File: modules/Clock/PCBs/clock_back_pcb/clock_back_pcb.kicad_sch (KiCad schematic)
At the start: 6 parts, among them J10 Conn_01x11_Pin, J11 Eurorack_2x8_Power, J9 Conn_01x08_Socket

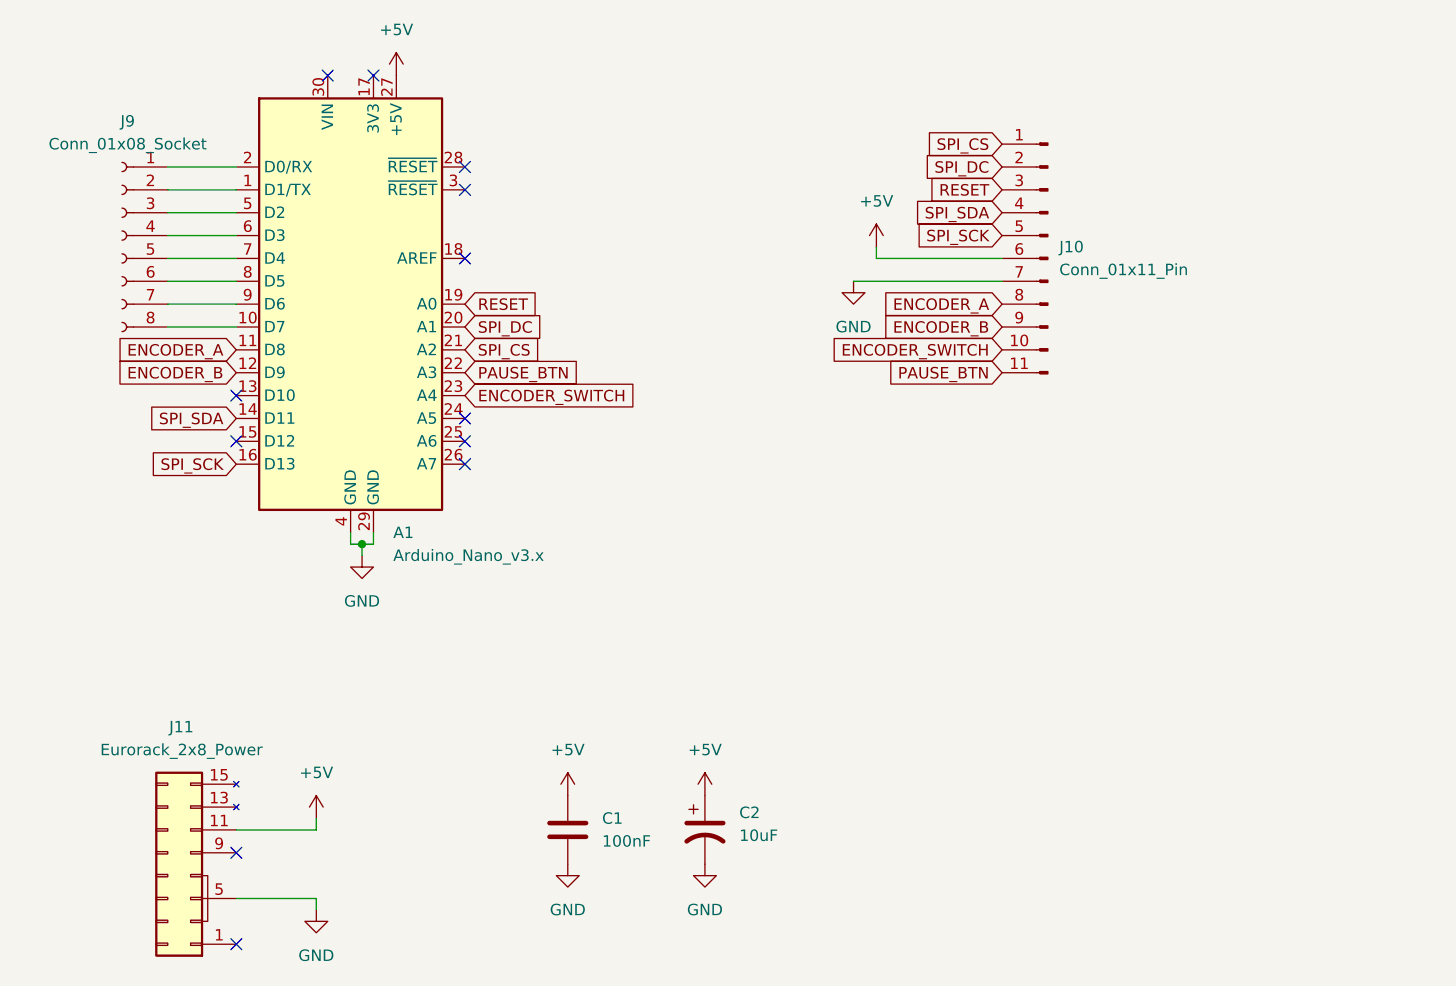
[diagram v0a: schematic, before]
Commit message: tweak clock faceplate
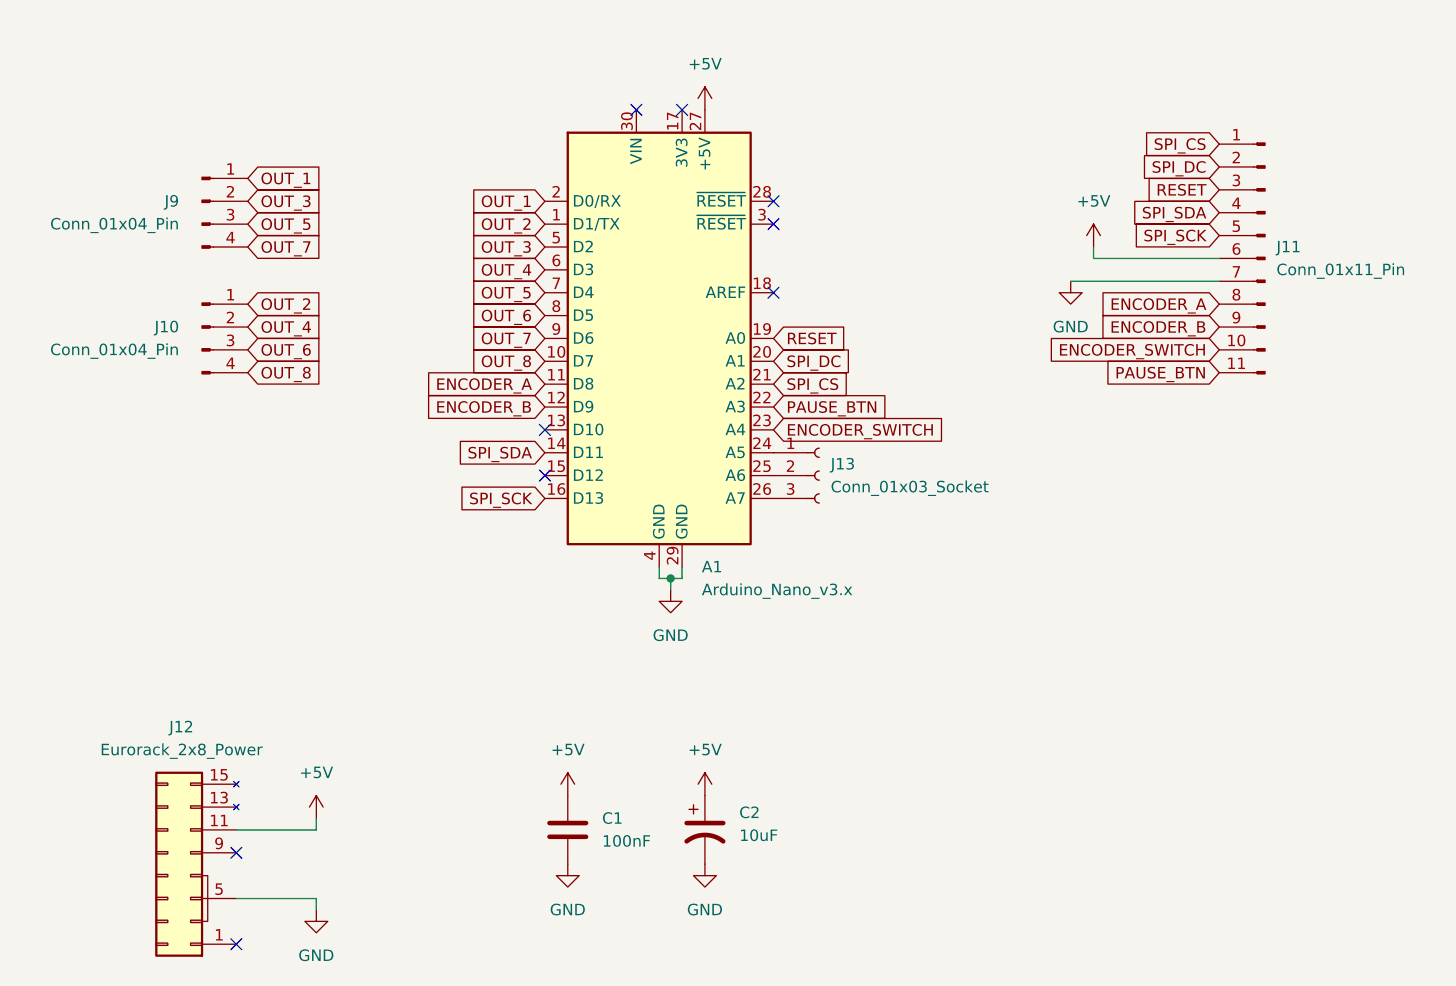
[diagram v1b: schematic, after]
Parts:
- removed J9: Conn_01x08_Socket, Connector_PinHeader_2.54mm:PinHeader_1x08_P2.54mm_Vertical, symbol Connector:Conn_01x08_Socket
- added J10, J9: Conn_01x04_Pin, Connector_PinHeader_2.54mm:PinHeader_1x04_P2.54mm_Vertical, symbol Connector:Conn_01x04_Pin
- added J13: Conn_01x03_Socket, Connector_PinHeader_2.54mm:PinHeader_1x03_P2.54mm_Vertical, symbol Connector:Conn_01x03_Socket
- renumbered J10 to J11, J11 to J12
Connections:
- net OUT_1: now reaches A1.2 (D0/RX)
- net OUT_1: now also J9.1 (Pin_1)
- net OUT_2: now reaches A1.1 (D1/TX)
- net OUT_2: now also J10.1 (Pin_1)
- net OUT_3: now reaches A1.5 (D2)
- net OUT_3: now also J9.2 (Pin_2)
- net OUT_4: now reaches A1.6 (D3)
- net OUT_4: now also J10.2 (Pin_2)
- net OUT_5: now reaches A1.7 (D4)
- net OUT_5: now also J9.3 (Pin_3)
- net OUT_6: now reaches A1.8 (D5)
- net OUT_6: now also J10.3 (Pin_3)
- net OUT_7: now reaches A1.9 (D6)
- net OUT_7: now also J9.4 (Pin_4)
- net OUT_8: now reaches A1.10 (D7)
- net OUT_8: now also J10.4 (Pin_4)
- net at A1.24 (A5): now also J13.1 (Pin_1)
- net at A1.25 (A6): now also J13.2 (Pin_2)
- net at A1.26 (A7): now also J13.3 (Pin_3)
- no-connect marks 12 -> 9
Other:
- moved on the sheet: A1, J11
